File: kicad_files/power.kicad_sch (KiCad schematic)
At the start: 22 parts, among them J11 Battery Connector, U11 LT1963AxST-3.3, U13 AP63205WU

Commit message: fix pyro adc
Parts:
- renumbered C51 to C49, C52 to C50, C53 to C51, C54 to C52, C55 to C53, C56 to C54, C57 to C55, C58 to C56, C59 to C57, J11 to J10
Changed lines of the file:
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@@
 		(dnp no)
 		(fields_autoplaced yes)
-		(property "Reference" "C59"
+		(property "Reference" "C57"
 			(at 161.29 127.0062 0)
 			(show_name no)
@@
 			(project "versorlite"
 				(path "/1a230af0-0a74-48f7-8607-b087121dda49/31c1824a-552d-4de4-ae9b-4526af07be04"
-					(reference "C59")
+					(reference "C57")
 					(unit 1)
 				)
@@
 		(dnp no)
 		(fields_autoplaced yes)
-		(property "Reference" "C53"
+		(property "Reference" "C51"
 			(at 46.9965 59.69 0)
 			(show_name no)
@@
 			(project "versorlite"
 				(path "/1a230af0-0a74-48f7-8607-b087121dda49/31c1824a-552d-4de4-ae9b-4526af07be04"
-					(reference "C53")
+					(reference "C51")
 					(unit 1)
 				)
@@
 		(dnp no)
 		(fields_autoplaced yes)
-		(property "Reference" "C57"
+		(property "Reference" "C55"
 			(at 107.95 134.6135 0)
 			(show_name no)
@@
 			(project "versorlite"
 				(path "/1a230af0-0a74-48f7-8607-b087121dda49/31c1824a-552d-4de4-ae9b-4526af07be04"
-					(reference "C57")
+					(reference "C55")
 					(unit 1)
 				)
@@
 		(dnp no)
 		(fields_autoplaced yes)
-		(property "Reference" "C52"
+		(property "Reference" "C50"
 			(at 46.9838 49.53 0)
 			(show_name no)
@@
 			(project "versorlite"
 				(path "/1a230af0-0a74-48f7-8607-b087121dda49/31c1824a-552d-4de4-ae9b-4526af07be04"
-					(reference "C52")
+					(reference "C50")
 					(unit 1)
 				)
@@
 		(dnp no)
 		(fields_autoplaced yes)
-		(property "Reference" "C58"
+		(property "Reference" "C56"
 			(at 151.13 126.9935 0)
 			(show_name no)
@@
 			(project "versorlite"
 				(path "/1a230af0-0a74-48f7-8607-b087121dda49/31c1824a-552d-4de4-ae9b-4526af07be04"
-					(reference "C58")
+					(reference "C56")
 					(unit 1)
 				)
@@
 		(dnp no)
 		(fields_autoplaced yes)
-		(property "Reference" "J11"
+		(property "Reference" "J10"
 			(at 226.06 149.8599 0)
 			(show_name no)
@@
 			(project "versorlite"
 				(path "/1a230af0-0a74-48f7-8607-b087121dda49/31c1824a-552d-4de4-ae9b-4526af07be04"
-					(reference "J11")
+					(reference "J10")
 					(unit 1)
 				)
@@
 		(dnp no)
 		(fields_autoplaced yes)
-		(property "Reference" "C56"
+		(property "Reference" "C54"
 			(at 74.93 129.5462 0)
 			(show_name no)
@@
 			(project "versorlite"
 				(path "/1a230af0-0a74-48f7-8607-b087121dda49/31c1824a-552d-4de4-ae9b-4526af07be04"
-					(reference "C56")
+					(reference "C54")
 					(unit 1)
 				)
@@
 		(dnp no)
 		(fields_autoplaced yes)
-		(property "Reference" "C54"
+		(property "Reference" "C52"
 			(at 45.7136 83.82 90)
 			(show_name no)
@@
 			(project "versorlite"
 				(path "/1a230af0-0a74-48f7-8607-b087121dda49/31c1824a-552d-4de4-ae9b-4526af07be04"
-					(reference "C54")
+					(reference "C52")
 					(unit 1)
 				)
@@
 		(dnp no)
 		(fields_autoplaced yes)
-		(property "Reference" "C55"
+		(property "Reference" "C53"
 			(at 45.7263 93.98 90)
 			(show_name no)
@@
 			(project "versorlite"
 				(path "/1a230af0-0a74-48f7-8607-b087121dda49/31c1824a-552d-4de4-ae9b-4526af07be04"
-					(reference "C55")
+					(reference "C53")
 					(unit 1)
 				)
@@
 		(dnp no)
 		(fields_autoplaced yes)
-		(property "Reference" "C51"
+		(property "Reference" "C49"
 			(at 23.5013 128.905 90)
 			(show_name no)
@@
 			(project "versorlite"
 				(path "/1a230af0-0a74-48f7-8607-b087121dda49/31c1824a-552d-4de4-ae9b-4526af07be04"
-					(reference "C51")
+					(reference "C49")
 					(unit 1)
 				)

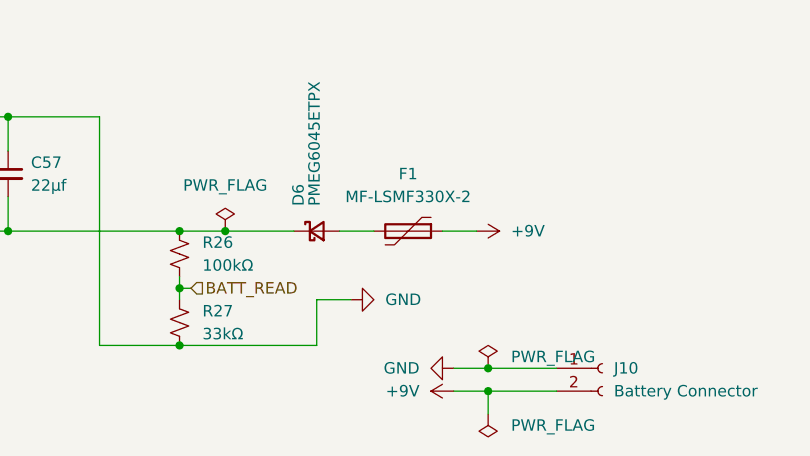
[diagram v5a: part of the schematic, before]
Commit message: connect pyro to fuse
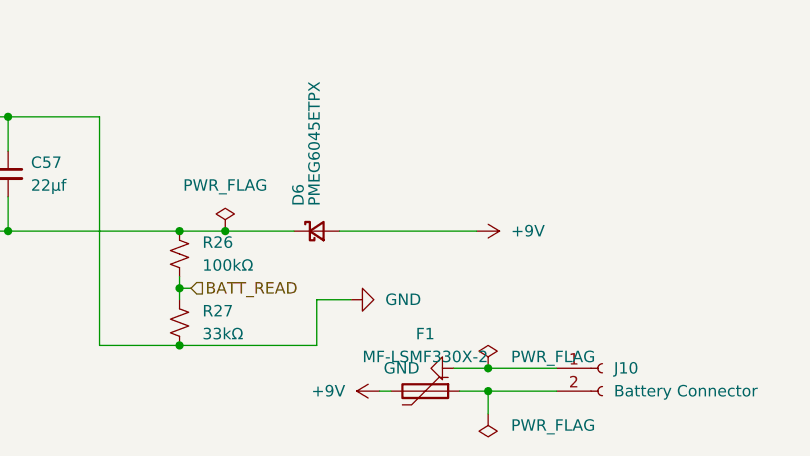
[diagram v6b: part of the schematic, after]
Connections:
- net +9V: now also D6.2 (A), F1.2; no longer F1.1, J10.2 (Pin_2)
- new net: F1.1, J10.2 (Pin_2)
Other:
- moved on the sheet: F1
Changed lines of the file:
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@@
+	)
+	(junction
+		(at 212.09 152.4)
+		(diameter 0)
+		(color 0 0 0 0)
 	)
 	(junction
@@
 	)
 	(junction
-		(at 212.09 152.4)
-		(diameter 0)
-		(color 0 0 0 0)
-	)
-	(junction
 		(at 40.64 100.33)
 		(diameter 0)
@@
 	(wire
 		(pts
-			(xy 195.58 134.62) (xy 199.39 134.62)
+			(xy 195.58 134.62) (xy 210.82 134.62)
 		)
 		(stroke
@@
 	(wire
 		(pts
-			(xy 208.28 152.4) (xy 212.09 152.4)
+			(xy 200.025 152.4) (xy 201.295 152.4)
 		)
 		(stroke
@@
 	(wire
 		(pts
+			(xy 208.915 152.4) (xy 212.09 152.4)
+		)
+		(stroke
+			(width 0)
+			(type default)
+		)
+	)
+	(wire
+		(pts
 			(xy 40.64 57.15) (xy 40.64 63.5)
 		)
@@
 		(pts
 			(xy 40.64 83.82) (xy 40.64 90.17)
-		)
-		(stroke
-			(width 0)
-			(type default)
-		)
-	)
-	(wire
-		(pts
-			(xy 207.01 134.62) (xy 210.82 134.62)
 		)
 		(stroke
@@
 	(symbol
 		(lib_id "power:+9V")
-		(at 208.28 152.4 90)
+		(at 200.025 152.4 90)
 		(unit 1)
 		(body_style 1)
@@
 		(fields_autoplaced yes)
 		(property "Reference" "#PWR092"
-			(at 212.09 152.4 0)
+			(at 203.835 152.4 0)
 			(hide yes)
 			(show_name no)
@@
 		)
 		(property "Value" "+9V"
-			(at 204.47 152.3999 90)
+			(at 196.215 152.3999 90)
 			(show_name no)
 			(do_not_autoplace no)
@@
 		)
 		(property "Footprint" ""
-			(at 208.28 152.4 0)
+			(at 200.025 152.4 0)
 			(hide yes)
 			(show_name no)
@@
 		)
 		(property "Datasheet" ""
-			(at 208.28 152.4 0)
+			(at 200.025 152.4 0)
 			(hide yes)
 			(show_name no)
@@
 		)
 		(property "Description" "Power symbol creates a global label with name \"+9V\""
-			(at 208.28 152.4 0)
+			(at 200.025 152.4 0)
 			(hide yes)
 			(show_name no)
@@
 	(symbol
 		(lib_id "Device:Polyfuse")
-		(at 203.2 134.62 270)
+		(at 205.105 152.4 270)
 		(unit 1)
 		(body_style 1)
@@
 		(fields_autoplaced yes)
 		(property "Reference" "F1"
-			(at 203.2 128.27 90)
+			(at 205.105 146.05 90)
 			(show_name no)
 			(do_not_autoplace no)
@@
 		)
 		(property "Value" "MF-LSMF330X-2"
-			(at 203.2 130.81 90)
+			(at 205.105 148.59 90)
 			(show_name no)
 			(do_not_autoplace no)
@@
 		)
 		(property "Footprint" "Fuse:Fuse_Bourns_MF-SM_7.98x5.44mm"
-			(at 198.12 135.89 0)
+			(at 200.025 153.67 0)
 			(hide yes)
 			(show_name no)
@@
 		)
 		(property "Datasheet" ""
-			(at 203.2 134.62 0)
+			(at 205.105 152.4 0)
 			(hide yes)
 			(show_name no)
@@
 		)
 		(property "Description" "Resettable fuse, polymeric positive temperature coefficient"
-			(at 203.2 134.62 0)
-			(hide yes)
-			(show_name no)
+			(at 205.105 152.4 0)
+			(hide yes)
+			(show_name no)

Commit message: jlcstuffs
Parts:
- L1: value CIGW252010GL4R7MNE, 4.7uH -> Inductor 4.7uH
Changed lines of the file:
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@@
 			)
 		)
-		(property "Value" "CIGW252010GL4R7MNE, 4.7uH"
+		(property "Value" "Inductor 4.7uH"
 			(at 93.98 142.24 90)
 			(show_name no)

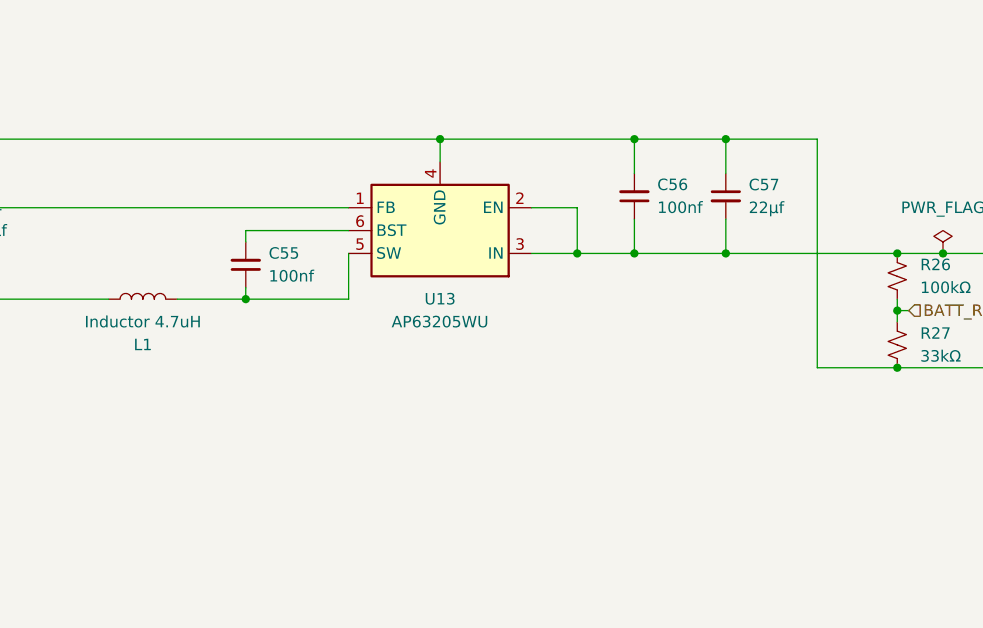
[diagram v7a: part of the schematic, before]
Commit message: switch buck converter
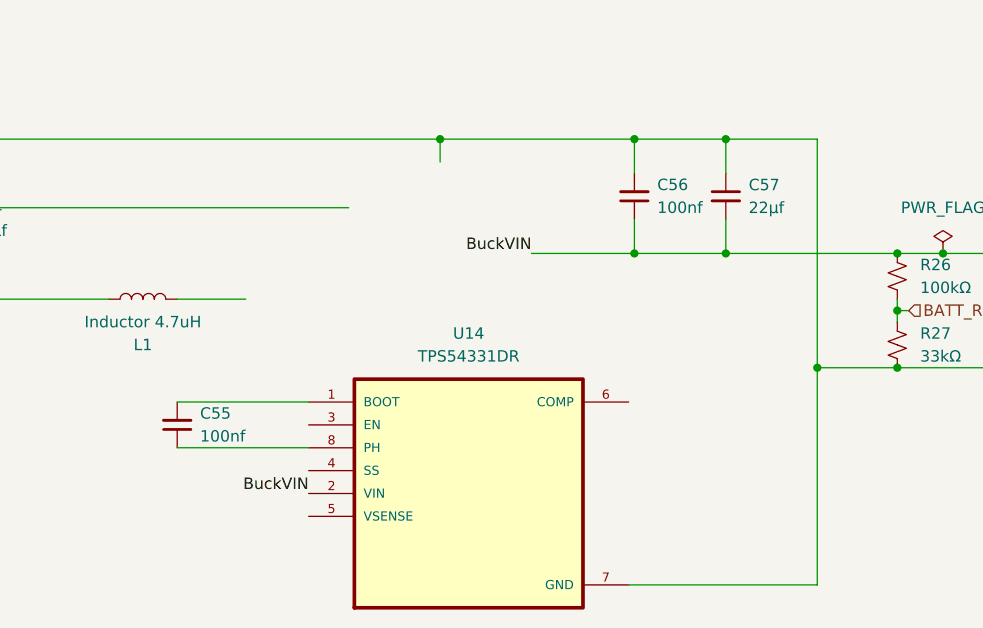
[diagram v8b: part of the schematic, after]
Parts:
- removed U13: AP63205WU, Package_TO_SOT_SMD:TSOT-23-6, symbol Regulator_Switching:AP63205WU
- added U14: TPS54331DR, footprints:SOIC127P599X175-8N, symbol TPS54331DR:TPS54331DR
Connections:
- net GND: now also U14.7 (GND)
- net BuckVIN: now reaches C56.1, C57.2, D6.1 (K), R26.1
- net BuckVIN: now also U14.2 (VIN)
- net at C55.1: now also U14.8 (PH); no longer L1.2
- net at C55.2: now also U14.1 (BOOT)
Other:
- moved on the sheet: C55
